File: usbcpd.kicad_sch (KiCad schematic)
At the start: 2 parts, among them J1 USB_C_Receptacle_USB2.0_14P, U1 STUSB4500QTR

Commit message: Add USBC material
Signed-off-by: sanyue <sanyue7th@gmail.com>
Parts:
- removed U1: STUSB4500QTR, Package_DFN_QFN:QFN-24-1EP_4x4mm_P0.5mm_EP2.7x2.7mm, symbol Interface_USB:STUSB4500QTR
- added C3, C5, C6: C1u 50V, Capacitor_SMD:C_0402_1005Metric, symbol Device:C
- added C4: C4u7 50V, Capacitor_SMD:C_0603_1608Metric, symbol Device:C
- added C7: C100n 50V, Capacitor_SMD:C_0402_1005Metric, symbol Device:C
- added D4, D7: ESDA25W, SOT65P210X110-3N, symbol aaafootprintlib:ESDA25W
- added D5: ESDA25P35-1U1M, TVS_ESDA25P35-1U1M, symbol aaafootprintlib:ESDA25P35-1U1M
- added D6: Zener_16-17V, Diode_SMD:D_SOD-123, symbol Device:D_Zener
- added J3: USB_C_Receptacle_USB2.0, MC-110LD [USB-C], symbol Connector:USB_C_Receptacle_USB2.0
- added JP3: Jumper_2_Open, Jumper:SolderJumper-2_P1.3mm_Open_TrianglePad1.0x1.5mm, symbol Jumper:Jumper_2_Open
- added R11: R100 125mW, Resistor_SMD:R_0402_1005Metric, symbol Device:R
- added R4: R10k 125mW, Resistor_SMD:R_0402_1005Metric, symbol Device:R
- added R7: R1k 125mW, Resistor_SMD:R_0402_1005Metric, symbol Device:R
- added R8: R22k 125mW, Resistor_SMD:R_0402_1005Metric, symbol Device:R
- added R9: R100k 125mW, Resistor_SMD:R_0402_1005Metric, symbol Device:R
- added U4, U6: STUSB4500QTR, QFN50P400X400X100-25N, symbol aaafootprintlib:STUSB4500LQTR
- added U5, U7: VBA4658, Package_SO:SO-8_3.9x4.9mm_P1.27mm, symbol aaafootprintlib:VBA4658
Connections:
- new net: C7.2, R11.2
- new net: D6.2 (A), R11.1, R8.2, R9.1, U5.2 (G1), U5.4 (G2)
- new net: D6.1 (K), R9.2, U5.1 (S1), U5.3 (S2)
- new net: U7.1 (S1), U7.3 (S2)
- new net: U7.5 (D2), U7.6 (D2)
- new net: U7.7 (D1), U7.8 (D1)
- new net 1A5: U4.14 (RP_1A5)
- new net 1V2: C5.1, U4.21 (VREG_1V2)
- new net 2V7: C3.1, U4.23 (VREG_2V7)
- new net 3A: U4.20 (RP_3A)
- new net ADDR0: U4.12 (ADDR0)
- new net ADDR1: U4.13 (ADDR1)
- new net CC1: D4.2, J3.A5 (CC1), U4.1 (CC1DB), U4.2 (CC1)
- new net CC2: D4.1, J3.B5 (CC2), U4.4 (CC2), U4.5 (CC2DB)
- new net COM_USBC_+: J3.A6 (D+), J3.B6 (D+)
- new net COM_USBC_-: J3.A7 (D-), J3.B7 (D-)
- new net GND: C3.2, C4.2, C5.2, C6.2, D4.3, D5.A, J3.A12B1 (GND), J3.A1B12 (GND), J3.S1 (SHIELD), R4.2, U4.10 (GND), U4.22 (VSYS), U4.25 (EXP)
- new net GPIO: U4.15 (GPIO)
- new net PP_INPUT: JP3.1 (A)
- new net aler: U4.19 (ALERT)
- new net attach: U4.11 (ATTACH)
- new net pp_usbc_vbus: C4.1, C6.1, D5.C, J3.A4B9 (VBUS), J3.A9B4 (VBUS), R7.2, U4.24 (VDD), U5.5 (D2), U5.6 (D2)
- new net reset: R4.1, U4.6 (RESET)
- new net scl: U4.7 (SCL)
- new net sda: U4.8 (SDA)
- new net vbus_disch: R7.1, U4.18 (VBUS_VS_DISCH)
- new net vbus_en: R8.1, U4.16 (VBUS_EN_SNK)
- new net vbus_fet_out: C7.1, JP3.2 (B), U5.7 (D1), U5.8 (D1)
- no-connect marks 0 -> 5
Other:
- note added: "(Lisha's Reference) STUSB4500 USB-PD Interface and Power Path Controller"
- note added: "cinnachancinnachan haihai! try to make the circuit i have above. u can copy the components, but do it a few/one at a time and understand the function of each component. remember u can click d while the component is selected to view the datasheet (the STUSB4500 chip) page 4 is very useful as it gives a description of each pin's function, and a helpful thing to do if you want more about a specific 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"
- note added: "reference material about USB Power Delivery intro to usb-c: https://www.allaboutcircuits.com/technical-articles/introduction-to-usb-type-c-which-pins-power-delivery-data-transfer/ longer, more technical: https://www.ti.com/lit/wp/slyy109b/slyy109b.pdf?ts=1741426598528&ref_url=https%253A%252F%252Fwww.google.com%252F"
- moved on the sheet: J1

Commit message: cinny work!!!!
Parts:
- added C8: C100n 50V, symbol Device:C
- added C9: C, symbol Device:C
- added D2: D_Zener, symbol Device:D_Zener
- added D8: ESDA25P35-1U1M, TVS_ESDA25P35-1U1M, symbol aaafootprintlib:ESDA25P35-1U1M
- added JP4: Jumper_2_Open, Jumper:SolderJumper-2_P1.3mm_Open_TrianglePad1.0x1.5mm, symbol Jumper:Jumper_2_Open
- added R1: R, symbol Device:R
- added R2, R3, R6: R1k 125mW, symbol Device:R
- added R5: R100 125mW, symbol Device:R
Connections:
- net GND: now also D7.3, J1.A12 (GND), J1.A1B1 (GND), J1.B1 (GND), J1.B12 (GND), J1.S1 (SHIELD), U6.10 (GND), U6.22 (VSYS), U6.25 (EXP), C9.2, D8.A, R1.2
- net at J1.A9 (VBUS), J1.B4 (VBUS), J1.B9 (VBUS): now also J1.A4B4 (VBUS), C9.1, D8.C; no longer J1.A4 (VBUS)
- net USB Data +: now reaches J1.A6 (D+)
- net USB Data +: now also J1.B6 (D+)
- net USB Data -: now reaches J1.A7 (D-)
- net USB Data -: now also J1.B7 (D-)
- net at U7.1 (S1), U7.3 (S2): now also D2.1 (K), R6.1
- net at U7.4 (G2): now also D2.2 (A), R3.2, R5.2, R6.2
- net at U7.7 (D1), U7.8 (D1): now also C8.1, JP4.2 (B)
- net at U6.1 (CC1DB): now also U6.2 (CC1)
- net at U6.16 (VBUS_EN_SNK): now also R3.1
- net at U6.18 (VBUS_VS_DISCH): now also R2.1
- net at U6.4 (CC2): now also U6.5 (CC2DB)
- net at U6.6 (RESET): now also R1.1
- new net: C8.2, R5.1
- new net pp_input: JP4.1 (A)
- no-connect marks 5 -> 8
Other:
- note added: "1a5"
- note added: "1v2"
- note added: "1v7"
- note added: "3a"
- note added: "ADDR0"
- note added: "ADDR1"
- note added: "CC1"
- note added: "CC2"
- note added: "GPIO"
- note added: "It can power switch, load switch, and DC-DC conversion"
- note added: "Protects electronic circuit from surges and transient spikes"
- note added: "alert"
- note added: "attach"
- note added: "pp_usbc_vbus"
- note added: "reset"
- note added: "scl"
- note added: "sda"
- note added: "snk enable"
- note added: "vbus_discharge"
- moved on the sheet: J1, U6, U7

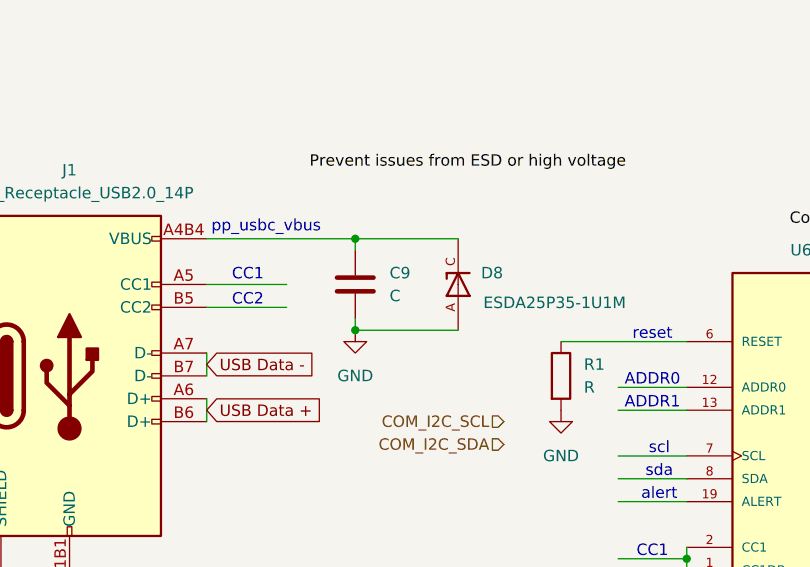
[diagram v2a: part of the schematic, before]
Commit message: added lcsc, datasheet, and footprint. couldn't find zener and polarized stuff tho
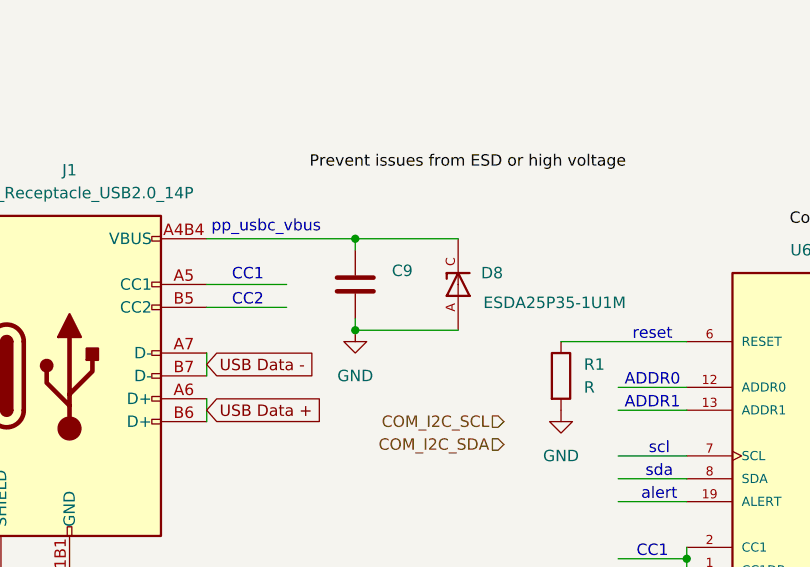
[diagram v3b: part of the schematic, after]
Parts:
- C8: footprint (none) -> Capacitor_SMD:C_0201_0603Metric; LCSC (none) -> C14663
- C9: footprint (none) -> Capacitor_SMD:C_0201_0603Metric; LCSC (none) -> C125977
- D2: footprint (none) -> Diode_SMD:Littelfuse_PolyZen-LS; LCSC (none) -> C5448546
- D7: LCSC (none) -> C2935152
- D8: LCSC (none) -> C19829649
- R1, R3, R5, R6: footprint (none) -> Resistor_SMD:R_0201_0603Metric; LCSC (none) -> C98220
- R2: footprint (none) -> Resistor_SMD:R_0201_0603Metric; LCSC (none) -> C5448546
- U6: LCSC (none) -> C2678061
- U7: LCSC (none) -> C416242
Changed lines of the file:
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@@
 			)
 		)
-		(property "Datasheet" "~"
+		(property "Datasheet" "https://www.lcsc.com/datasheet/lcsc_datasheet_2410010403_STMicroelectronics-ESDA25W_C2935152.pdf"
 			(at 49.53 144.78 0)
 			(effects
@@
 		)
 		(property "Description" ""
+			(at 49.53 144.78 0)
+			(effects
+				(font
+					(size 1.27 1.27)
+				)
+				(hide yes)
+			)
+		)
+		(property "LCSC" "C2935152"
 			(at 49.53 144.78 0)
 			(effects
@@
 			)
 		)
-		(property "Footprint" ""
+		(property "Footprint" "Capacitor_SMD:C_0201_0603Metric"
 			(at 244.8052 93.98 0)
 			(effects
@@
 			)
 		)
-		(property "Datasheet" "~"
+		(property "Datasheet" "https://www.lcsc.com/datasheet/lcsc_datasheet_2211101700_YAGEO-CC0603KRX7R9BB104_C14663.pdf"
 			(at 243.84 90.17 0)
 			(effects
@@
 		)
 		(property "Description" "Unpolarized capacitor"
+			(at 243.84 90.17 0)
+			(effects
+				(font
+					(size 1.27 1.27)
+				)
+				(hide yes)
+			)
+		)
+		(property "LCSC" "C14663"
 			(at 243.84 90.17 0)
 			(effects
@@
 			)
 		)
-		(property "Datasheet" "~"
+		(property "Datasheet" "https://www.lcsc.com/datasheet/lcsc_datasheet_2409300832_VBsemi-Elec-VBA4658_C416242.pdf"
 			(at 224.79 80.01 0)
 			(effects
@@
 			)
 		)
+		(property "LCSC" "C416242"
+			(at 224.79 80.01 0)
+			(effects
+				(font
+					(size 1.27 1.27)
+				)
+				(hide yes)
+			)
+		)
 		(pin "1"
 		)
@@
 		(on_board yes)
 		(dnp no)
-		(fields_autoplaced yes)
 		(property "Reference" "C9"
-			(at 71.12 86.3599 0)
+			(at 71.374 86.106 0)
 			(effects
 				(font
@@
 		)
 		(property "Value" "C"
-			(at 71.12 88.8999 0)
+			(at 72.644 88.646 0)
 			(effects
 				(font
@@
 				)
 				(justify left)
-			)
-		)
-		(property "Footprint" ""
+				(hide yes)
+			)
+		)
+		(property "Footprint" "Capacitor_SMD:C_0201_0603Metric"
 			(at 68.2752 91.44 0)
 			(effects
@@
 			)
 		)
-		(property "Datasheet" "~"
+		(property "Datasheet" "https://www.lcsc.com/datasheet/lcsc_datasheet_2409241209_Nichicon-UWT1H221MNL1GS_C125977.pdf"
 			(at 67.31 87.63 0)
 			(effects
@@
 			)
 		)
+		(property "LCSC" "C125977"
+			(at 67.31 87.63 0)
+			(effects
+				(font
+					(size 1.27 1.27)
+				)
+				(hide yes)
+			)
+		)
 		(pin "2"
 		)
@@
 			)
 		)
-		(property "Footprint" ""
+		(property "Footprint" "Resistor_SMD:R_0201_0603Metric"
 			(at 165.862 110.49 90)
 			(effects
@@
 			)
 		)
-		(property "Datasheet" "~"
+		(property "Datasheet" "https://www.lcsc.com/datasheet/lcsc_datasheet_2304140030_YAGEO-RC0603FR-0710KL_C98220.pdf"
 			(at 167.64 110.49 0)
 			(effects
@@
 		)
 		(property "Description" "Resistor"
+			(at 167.64 110.49 0)
+			(effects
+				(font
+					(size 1.27 1.27)
+				)
+				(hide yes)
+			)
+		)
+		(property "LCSC" "C98220"
 			(at 167.64 110.49 0)
 			(effects
@@
 			)
 		)
-		(property "Footprint" ""
+		(property "Footprint" "Resistor_SMD:R_0201_0603Metric"
 			(at 224.282 101.6 90)
 			(effects
@@
 			)
 		)
-		(property "Datasheet" "~"
+		(property "Datasheet" "https://www.lcsc.com/datasheet/lcsc_datasheet_2304140030_YAGEO-RC0603FR-0710KL_C98220.pdf"
 			(at 226.06 101.6 0)
 			(effects
@@
 		)
 		(property "Description" "Resistor"
+			(at 226.06 101.6 0)
+			(effects
+				(font
+					(size 1.27 1.27)
+				)
+				(hide yes)
+			)
+		)
+		(property "LCSC" "C98220"
 			(at 226.06 101.6 0)
 			(effects
@@
 			)
 		)
-		(property "Footprint" ""
+		(property "Footprint" "Resistor_SMD:R_0201_0603Metric"
 			(at 88.392 97.79 90)
 			(effects
@@
 			)
 		)
-		(property "Datasheet" "~"
+		(property "Datasheet" "https://www.lcsc.com/datasheet/lcsc_datasheet_2304140030_YAGEO-RC0603FR-0710KL_C98220.pdf"
 			(at 90.17 97.79 0)
 			(effects
@@
 		)
 		(property "Description" "Resistor"
+			(at 90.17 97.79 0)
+			(effects
+				(font
+					(size 1.27 1.27)
+				)
+				(hide yes)
+			)
+		)
+		(property "LCSC" "C98220"
 			(at 90.17 97.79 0)
 			(effects
@@
 			)
 		)
-		(property "Datasheet" "~"
+		(property "Datasheet" "https://www.lcsc.com/datasheet/lcsc_datasheet_2411121028_TECH-PUBLIC-ESDA25P35-1U1M_C19829649.pdf"
 			(at 78.74 87.63 0)
 			(effects
@@
 			)
 		)
+		(property "LCSC" "  C19829649"
+			(at 83.566 83.566 90)
+			(effects
+				(font
+					(size 1.27 1.27)
+				)
+				(hide yes)
+			)
+		)
 		(pin "C"
 		)
@@
 			)
 		)
-		(property "Footprint" ""
+		(property "Footprint" "Diode_SMD:Littelfuse_PolyZen-LS"
 			(at 220.98 101.6 0)
 			(effects
@@
 			)
 		)
-		(property "Datasheet" "~"
+		(property "Datasheet" "https://www.lcsc.com/datasheet/lcsc_datasheet_2410121247_High-Diode-1SMA4750A_C5448546.pdf"
 			(at 220.98 101.6 0)
 			(effects
@@
 		(property "Description" "Zener diode"
 			(at 220.98 101.6 0)
+			(effects
+				(font
+					(size 1.27 1.27)
+				)
+				(hide yes)
+			)
+		)
+		(property "LCSC" "C5448546"
+			(at 220.98 101.6 90)
 			(effects
 				(font
@@
 			)
 		)
-		(property "Footprint" ""
+		(property "Footprint" "Resistor_SMD:R_0201_0603Metric"
 			(at 242.062 101.6 90)
 			(effects
@@
 			)
 		)
-		(property "Datasheet" "~"
+		(property "Datasheet" "https://www.lcsc.com/datasheet/lcsc_datasheet_2304140030_YAGEO-RC0603FR-0710KL_C98220.pdf"
 			(at 243.84 101.6 0)
 			(effects
@@
 			)
 		)
+		(property "LCSC" "C98220"
+			(at 243.84 101.6 0)
+			(effects
+				(font
+					(size 1.27 1.27)
+				)
+				(hide yes)
+			)
+		)
 		(pin "1"
 		)
@@
 			)
 		)
-		(property "Footprint" ""
+		(property "Footprint" "Resistor_SMD:R_0201_0603Metric"
 			(at 167.64 103.378 90)
 			(effects
@@
 			)
 		)
-		(property "Datasheet" "~"
+		(property "Datasheet" "https://www.lcsc.com/datasheet/lcsc_datasheet_2410121247_High-Diode-1SMA4750A_C5448546.pdf"
 			(at 167.64 101.6 0)
 			(effects
@@
 		(property "Description" "Resistor"
 			(at 167.64 101.6 0)
+			(effects
+				(font
+					(size 1.27 1.27)
+				)
+				(hide yes)
+			)
+		)
+		(property "LCSC" "C5448546"
+			(at 167.64 101.6 90)
 			(effects
 				(font
@@
 			)
 		)
-		(property "Datasheet" "~"
+		(property "Datasheet" "https://www.lcsc.com/datasheet/lcsc_datasheet_2106070703_STMicroelectronics-STUSB4500QTR_C2678061.pdf"
 			(at 127 114.3 0)
 			(effects
@@
 			(at 127 114.3 0)
 			(effects
+				(font
+					(size 1.27 1.27)
+				)
+				(hide yes)
+			)
+		)
+		(property "LCSC" "C2678061"
+			(at 127 114.3 0)
+			(effects

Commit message: Add light-white
Signed-off-by: sanyue <sanyue7th@gmail.com>
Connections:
- net pp_usbc_vbus: now also C9.1, D8.C, J1.A4B4 (VBUS), J1.A9 (VBUS), J1.B4 (VBUS), J1.B9 (VBUS)
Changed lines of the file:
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@@
-		)
-	)
-	(text "pp_usbc_vbus"
-		(exclude_from_sim no)
-		(at 57.404 81.28 0)
-		(effects
-			(font
-				(size 1.27 1.27)
-			)
 		)
 	)
@@
 		)
 	)
+	(label "pp_usbc_vbus"
+		(at 53.34 82.55 0)
+		(effects
+			(font
+				(size 1.27 1.27)
+			)
+			(justify left bottom)
+		)
+	)
 	(label "2V7"
 		(at 58.42 -19.05 0)
@@
 		(effects
 			(font
-				(size 1.27 1.27)
-			)
-			(justify left bottom)
-		)
-	)
-	(label "Prevent issues from ESD or high voltage"
-		(at 62.23 74.93 0)
-		(effects
-			(font

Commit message: cinna 4 more circuit
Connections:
- net ADDR0: now also U6.12 (ADDR0)
- net ADDR1: now also U6.13 (ADDR1)
- net CC1: now also J1.A5 (CC1), U6.1 (CC1DB), U6.2 (CC1)
- net CC2: now also J1.B5 (CC2), U6.4 (CC2), U6.5 (CC2DB)
- net GPIO: now also U6.15 (GPIO)
- net attach: now also U6.11 (ATTACH)
- net pp_usbc_vbus: now also R2.2, U6.24 (VDD), U7.5 (D2), U7.6 (D2)
- net reset: now also R1.1, U6.6 (RESET)
- net scl: now also U6.7 (SCL)
- net sda: now also U6.8 (SDA)
- net snk_enable: now reaches R3.1, U6.16 (VBUS_EN_SNK)
- net 1a5: now reaches U6.14 (RP_1A5)
- net alert: now reaches U6.19 (ALERT)
- net 3a: now reaches U6.20 (RP_3A)
- net 1v2: now reaches U6.21 (VREG_1V2)
- net 1v7: now reaches U6.23 (VREG_2V7)
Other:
- note removed: "1a5"
- note removed: "1v2"
- note removed: "1v7"
- note removed: "3a"
- note removed: "ADDR0"
- note removed: "ADDR1"
- note removed: "GPIO"
- note removed: "alert"
- note removed: "attach"
- note removed: "pp_usbc_vbus"
- note removed: "reset"
- note removed: "scl"
- note removed: "sda"
- note removed: "snk enable"
- note removed: "vbus_discharge"
